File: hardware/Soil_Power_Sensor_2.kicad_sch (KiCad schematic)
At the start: 46 parts, among them J1 DC050-T, Q1 AO3401A, Q2 AO3401A, Q3 AO3400A, U1 BQ24210DQCR, U2 TPS63900, U3 TPS631000DRLR

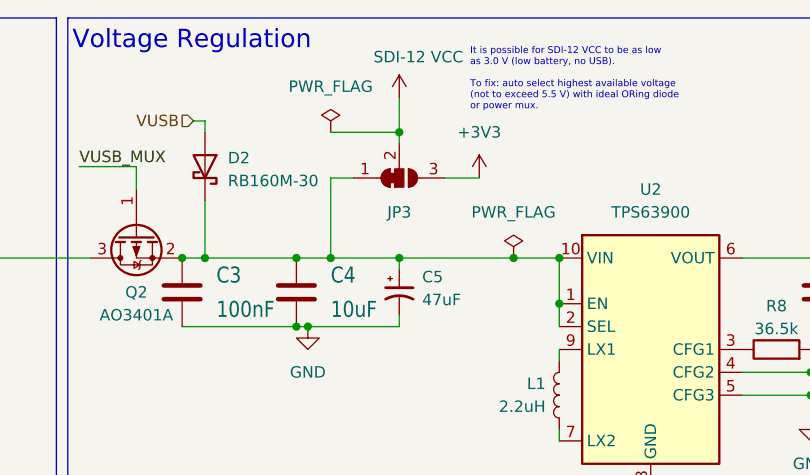
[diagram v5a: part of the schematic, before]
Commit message: WIP, button swap, single long header
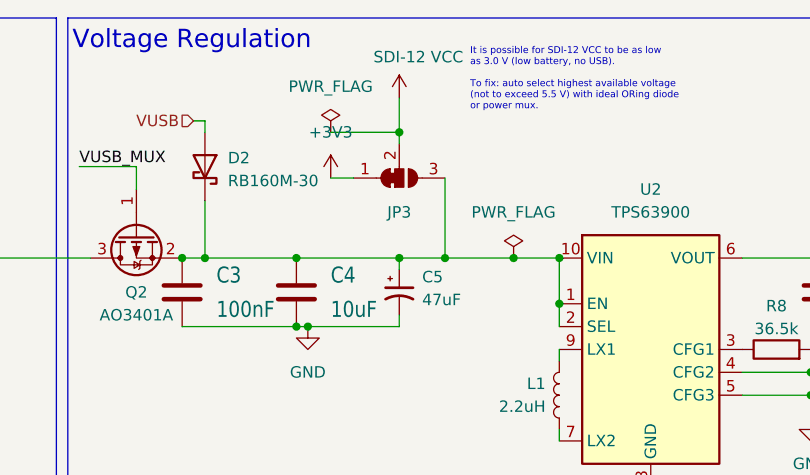
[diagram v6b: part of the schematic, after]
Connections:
- net +3V3: now also JP3.1 (A); no longer JP3.3 (B)
- net at C3.1, C4.1, C5.1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: now also JP3.3 (B); no longer JP3.1 (A)
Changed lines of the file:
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@@
+	)
+	(junction
+		(at 199.39 39.37)
+		(diameter 0)
+		(color 0 0 0 0)
 	)
 	(junction
@@
 	(junction
 		(at 276.86 30.48)
-		(diameter 0)
-		(color 0 0 0 0)
-	)
-	(junction
-		(at 186.69 39.37)
 		(diameter 0)
 		(color 0 0 0 0)
@@
 	(wire
 		(pts
-			(xy 186.69 39.37) (xy 194.31 39.37)
-		)
-		(stroke
-			(width 0)
-			(type default)
-		)
-	)
-	(wire
-		(pts
-			(xy 194.31 39.37) (xy 207.01 39.37)
+			(xy 194.31 39.37) (xy 199.39 39.37)
 		)
 		(stroke
@@
 	(wire
 		(pts
+			(xy 199.39 30.48) (xy 199.39 39.37)
+		)
+		(stroke
+			(width 0)
+			(type default)
+		)
+	)
+	(wire
+		(pts
 			(xy 240.03 57.15) (xy 240.03 54.61)
 		)
@@
 	(wire
 		(pts
-			(xy 186.69 30.48) (xy 186.69 39.37)
-		)
-		(stroke
-			(width 0)
-			(type default)
-		)
-	)
-	(wire
-		(pts
 			(xy 212.09 58.42) (xy 212.09 59.69)
 		)
@@
 	(wire
 		(pts
-			(xy 182.88 39.37) (xy 186.69 39.37)
+			(xy 182.88 39.37) (xy 194.31 39.37)
+		)
+		(stroke
+			(width 0)
+			(type default)
+		)
+	)
+	(wire
+		(pts
+			(xy 199.39 39.37) (xy 207.01 39.37)
 		)
 		(stroke
@@
 		(pts
 			(xy 194.31 25.4) (xy 194.31 26.67)
-		)
-		(stroke
-			(width 0)
-			(type default)
-		)
-	)
-	(wire
-		(pts
-			(xy 199.39 30.48) (xy 203.2 30.48)
 		)
 		(stroke
@@
 	(symbol
 		(lib_id "power:+3V3")
-		(at 203.2 30.48 0)
+		(at 186.69 30.48 0)
 		(unit 1)
 		(exclude_from_sim no)
@@
 		(dnp no)
 		(property "Reference" "#PWR02"
-			(at 203.2 34.29 0)
+			(at 186.69 34.29 0)
 			(effects
 				(font
@@
 		)
 		(property "Value" "+3V3"
-			(at 203.2 25.4 0)
+			(at 186.69 25.4 0)
 			(effects
 				(font
@@
 		)
 		(property "Footprint" ""
-			(at 203.2 30.48 0)
+			(at 186.69 30.48 0)
 			(effects
 				(font
@@
 		)
 		(property "Datasheet" ""
-			(at 203.2 30.48 0)
+			(at 186.69 30.48 0)
 			(effects
 				(font
@@
 		)
 		(property "Description" "Power symbol creates a global label with name \"+3V3\""
-			(at 203.2 30.48 0)
-			(effects
-				(font
+			(at 186.69 30.48 0)
+			(effects
+				(font

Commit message: 3.1.0 tidy layout, single header
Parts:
- removed TP1: V_{BUS}, TestPoint:TestPoint_Pad_D1.5mm, symbol Connector:TestPoint
- removed TP2: V_{BAT}/2, TestPoint:TestPoint_Pad_D1.5mm, symbol Connector:TestPoint
- removed U3: TPS631000DRLR, Soil Power Sensor:TPS631000DRLR_TEX, symbol Soil Power Sensor-eagle-import:TPS631000DRLR
- JP3: footprint Connector_PinHeader_2.54mm:PinHeader_1x03_P2.54mm_Vertical -> Jumper:SolderJumper-3_P1.3mm_Open_RoundedPad1.0x1.5mm; now left out of the parts list
- L1: footprint Inductor_SMD:L_0805_2012Metric -> Inductor_SMD:L_TechFuse_SL0420; LCSC C1043 -> C22463806; MFC (none) -> TECHFUSE; MPN CMI201209U2R2KT -> SL0420-2R2M
- R9: value 21.5k -> 22k
- TH1: now not fitted
- U1: footprint Package_SON:WSON-10-1EP_2x3mm_P0.5mm_EP0.84x2.4mm_ThermalVias -> Package_SON:WSON-10-1EP_2x3mm_P0.5mm_EP0.84x2.4mm
- U2: footprint Package_SON:WSON-10-1EP_2.5x2.5mm_P0.5mm_EP1.2x2mm_ThermalVias -> Package_SON:WSON-10-1EP_2.5x2.5mm_P0.5mm_EP1.2x2mm
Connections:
- no-connect marks 8 -> 0
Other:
- note added: "VDPM left floating / high Z to use battery tracking mode, can be between 1k 10k. 7.32 kOhm enabled with USB."
- note removed: "Active high enable. Mode: set low for auto (power saving) mode."
- note removed: "VDPM left floating to use battery tracking mode, can be between 1k 10k. 7.32 kOhm enabled with USB."
